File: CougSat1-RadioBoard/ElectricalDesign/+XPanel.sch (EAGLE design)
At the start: 65 parts, among them J1 ADCS Connector, J2 Low Gain +, J3 Low Gain -, J4 Low Gain Coax, J5 GPS Coax, J6 EPS Connector, U1 AD8515, U3 AD7291

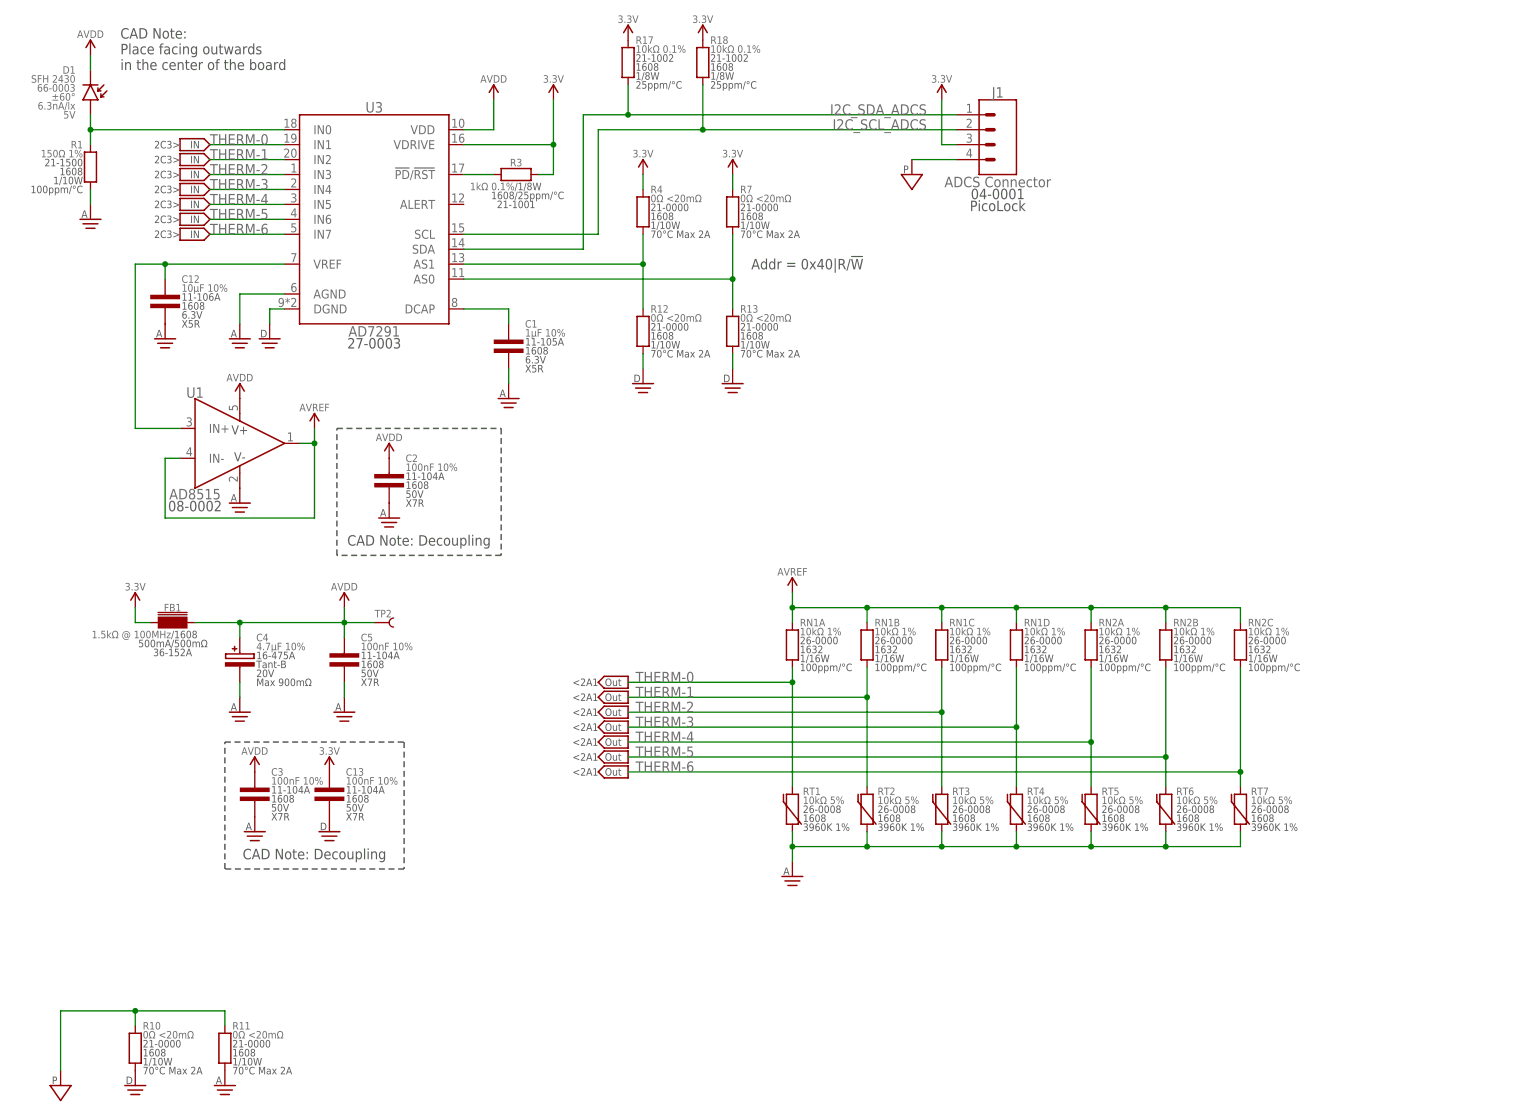
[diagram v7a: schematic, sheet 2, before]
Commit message: Moved Capacitors
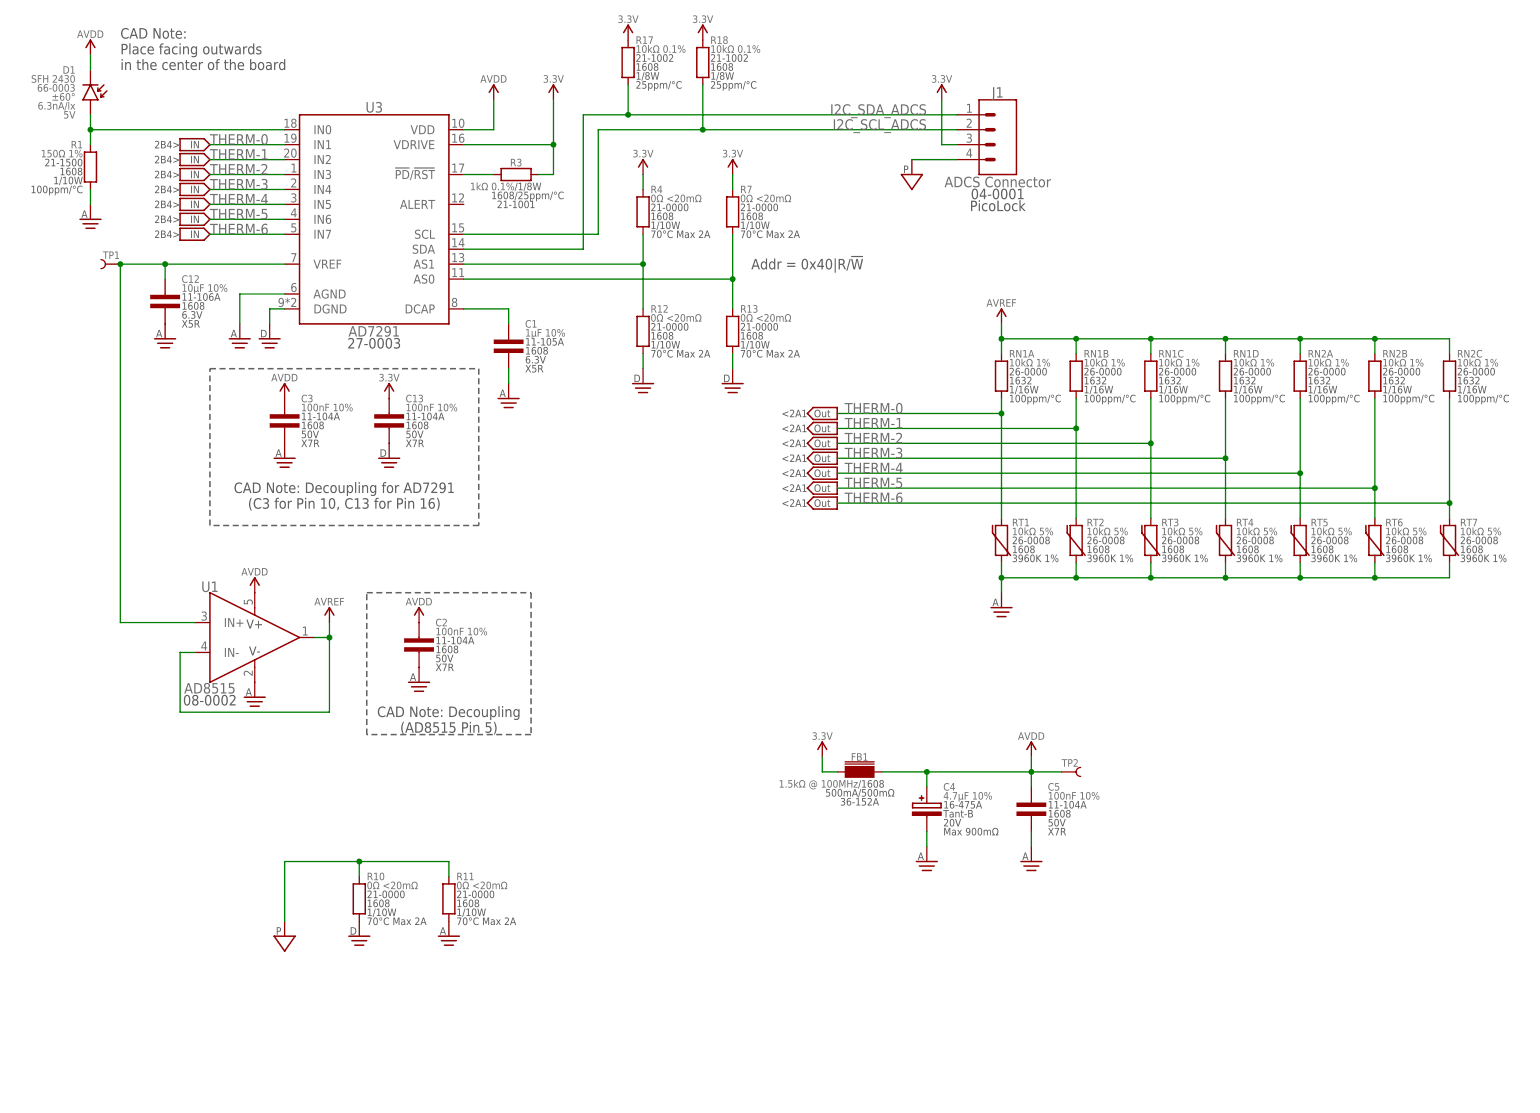
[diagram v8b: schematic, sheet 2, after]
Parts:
- added TP1: TEST_POINT-SMD-C-1.25, CougsInSpace-Connectors:TEST_POINT-SMD-C-1.25
- TP2: value TEST_POINT-THT-0.7 -> TEST_POINT-SMD-C-1.25; device CougsInSpace-Connectors:TEST_POINT-THT-0.7 -> CougsInSpace-Connectors:TEST_POINT-SMD-C-1.25
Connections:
- net AVREF_UNBUF: now also TP1.1
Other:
- note added: "2B4>"
- note added: "CAD Note: Decoupling (AD8515 Pin 5)"
- note added: "CAD Note: Decoupling for AD7291 (C3 for Pin 10, C13 for Pin 16)"
- note removed: "2C3>"
- note removed: "CAD Note: Decoupling"
- moved on the sheet: C13, C2, C3, C4, C5, FB1, R10, R11, RN1A, RN1B, RN1C, RN1D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
